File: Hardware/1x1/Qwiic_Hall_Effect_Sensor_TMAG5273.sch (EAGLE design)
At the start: 7 parts, among them J1 QWIIC_RIGHT_ANGLE, J2 QWIIC_RIGHT_ANGLE, U1 TMAG5273

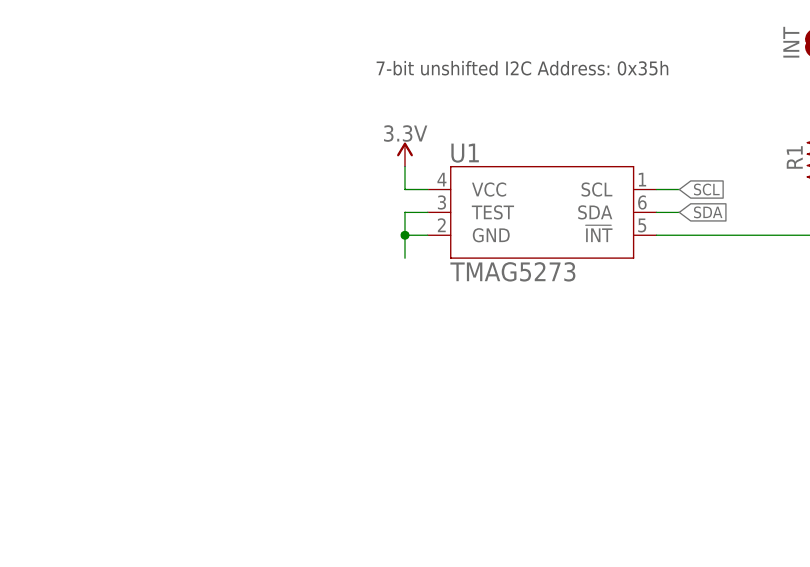
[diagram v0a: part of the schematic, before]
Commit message: Restructured file folders for new board
Added the micro folder and schematic to the project. Moved the 1x1 board into its own file folder.
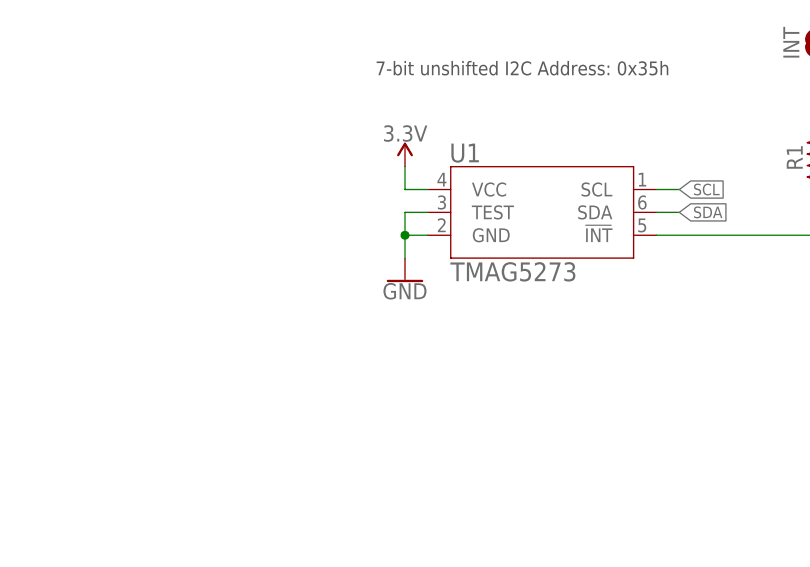
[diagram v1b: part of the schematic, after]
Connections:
- removed net N$1: U1.GND, U1.TEST
- net GND: now also U1.GND, U1.TEST
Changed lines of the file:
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@@
 <part name="SUPPLY5" library="SparkFun-PowerSymbols" deviceset="3.3V" device=""/>
 <part name="GND3" library="SparkFun-PowerSymbols" deviceset="GND" device=""/>
+<part name="GND4" library="SparkFun-PowerSymbols" deviceset="GND" device=""/>
 </parts>
 <sheets>
@@
 <attribute name="VALUE" x="175.26" y="124.206" size="1.778" layer="96" font="vector" align="top-center"/>
 </instance>
+<instance part="GND4" gate="1" x="106.68" y="127" smashed="yes">
+<attribute name="VALUE" x="106.68" y="126.746" size="1.778" layer="96" font="vector" align="top-center"/>
+</instance>
 </instances>
 <busses>
@@
 <wire x1="175.26" y1="127" x2="175.26" y2="128.016" width="0.1524" layer="91"/>
 </segment>
-</net>
-<net name="N$1" class="0">
 <segment>
 <pinref part="U1" gate="A" pin="TEST"/>
@@
 <wire x1="106.68" y1="132.08" x2="106.68" y2="129.54" width="0.1524" layer="91"/>
 <junction x="106.68" y="132.08"/>
+<pinref part="GND4" gate="1" pin="GND"/>
 </segment>
 </net>

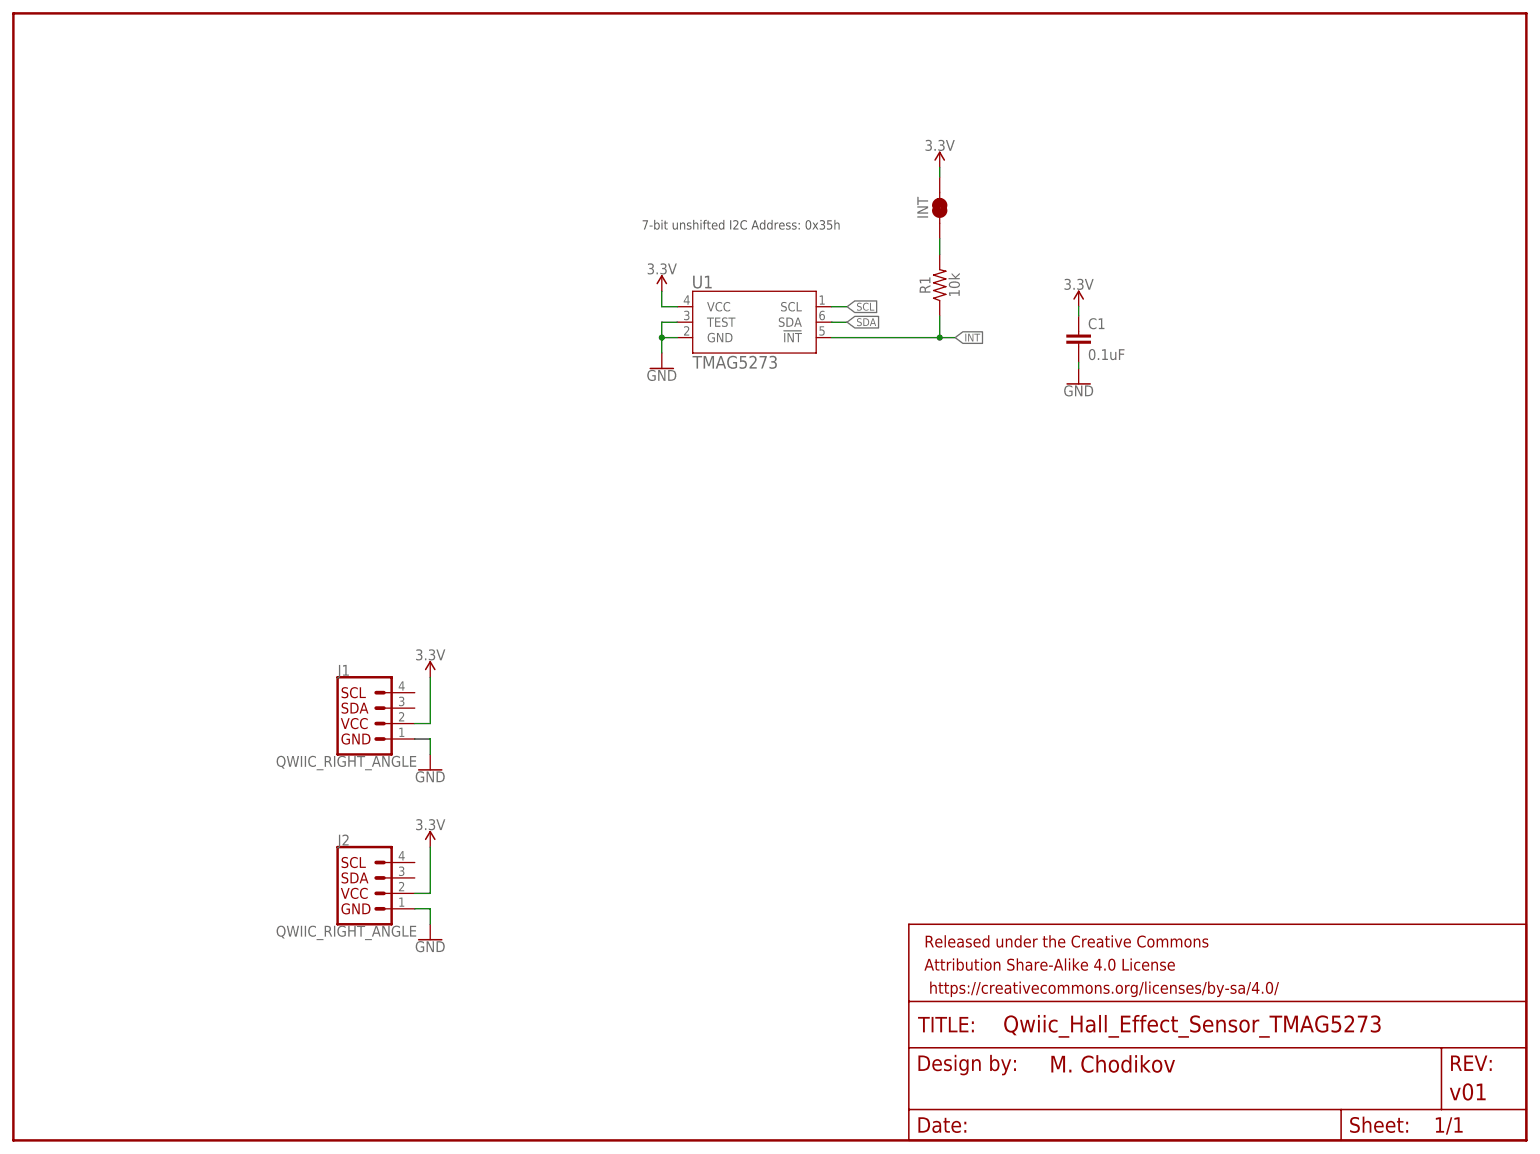
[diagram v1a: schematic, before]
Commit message: Completed schematic and routing
Need to finish aesthetics and dimensions to layout. Almost ready for review.
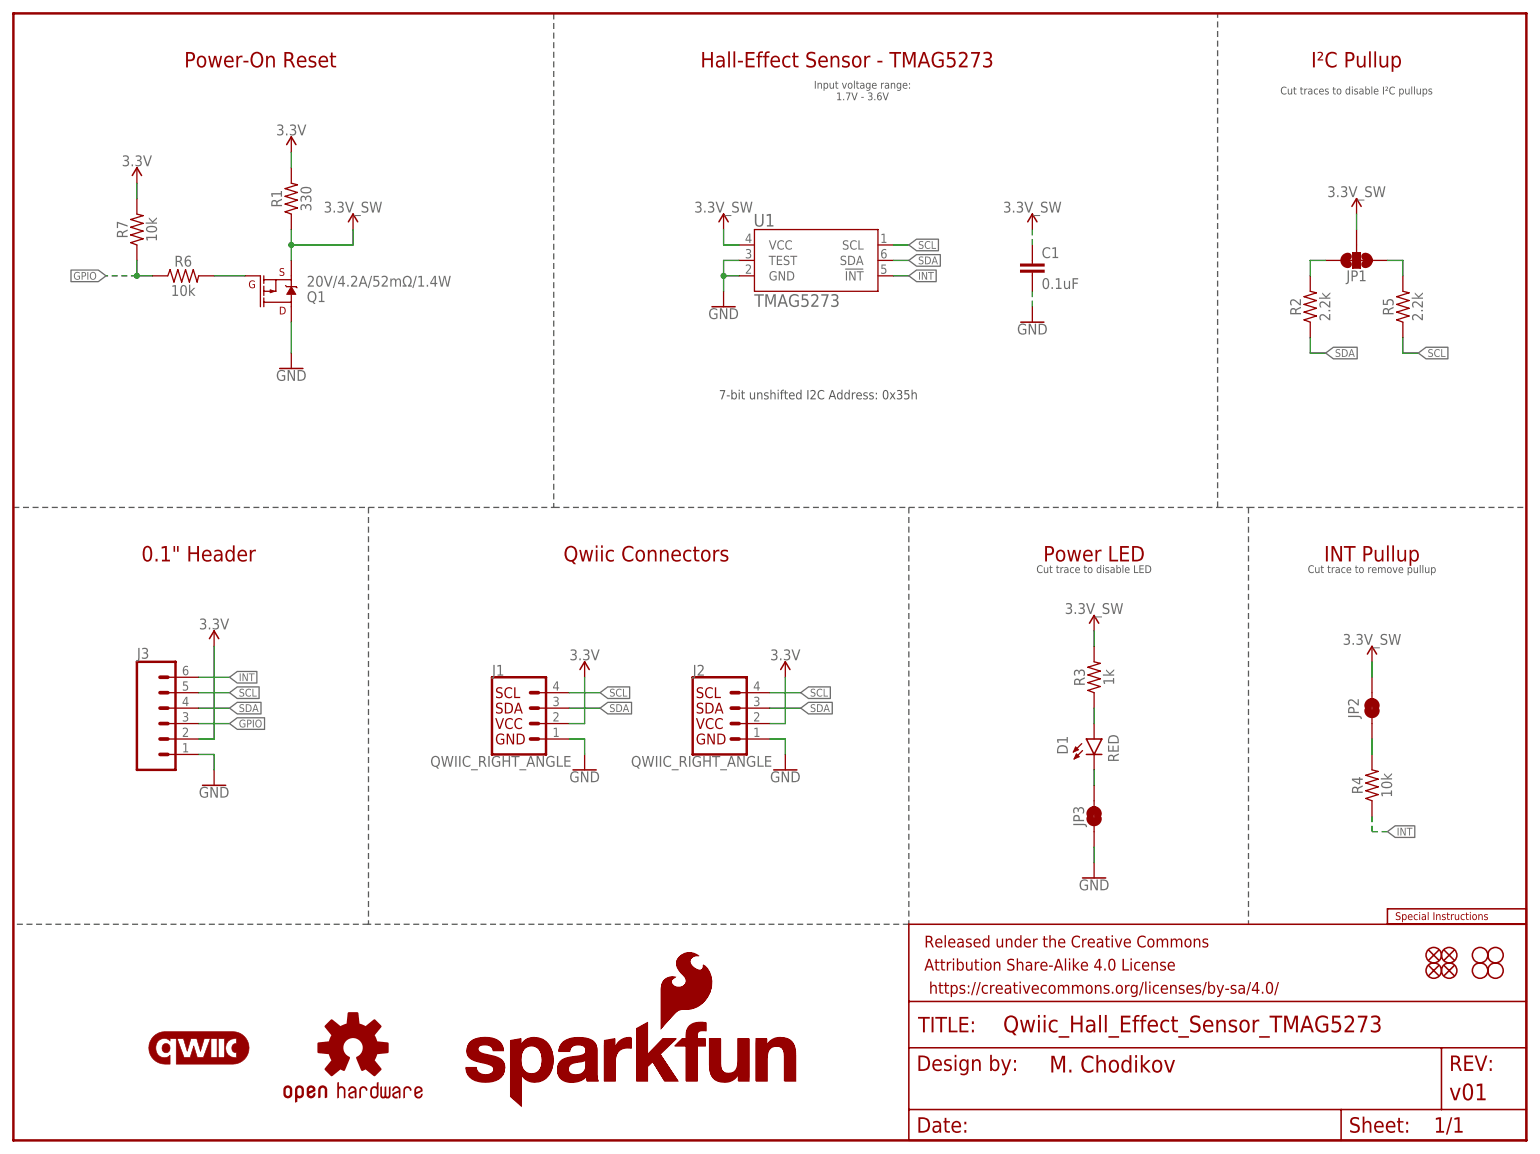
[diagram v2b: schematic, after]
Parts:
- removed INT: JUMPER-SMT_2_NC_TRACE_SILK, SparkFun-Jumpers:JUMPER-SMT_2_NC_TRACE_SILK
- added D1: RED, SparkFun-LED:LED-RED0603
- added FD1, FD2, FD3, FD4: FIDUCIAL1X2, SparkFun-Aesthetics:FIDUCIAL1X2
- added H1, H2, H3, H4: STAND-OFF, SparkFun-Hardware:STAND-OFF
- added J3: (no value), SparkFun-Connectors:CONN_06NO_SILK_FEMALE_PTH
- added JP1: JUMPER-SMT_3_2-NC_TRACE_SILK, SparkFun-Jumpers:JUMPER-SMT_3_2-NC_TRACE_SILK
- added JP2, JP3: JUMPER-SMT_2_NC_TRACE_SILK, SparkFun-Jumpers:JUMPER-SMT_2_NC_TRACE_SILK
- added LOGO1: OSHW-LOGOS, SparkFun-Aesthetics:OSHW-LOGOS
- added LOGO2: SFE_LOGO_NAME_FLAME.1_INCH, SparkFun-Aesthetics:SFE_LOGO_NAME_FLAME.1_INCH
- added LOGO3: QWIIC_LOGO_CONNECTOR, SparkFun-Aesthetics:QWIIC_LOGO_CONNECTOR
- added LOGO4: SFE_LOGO_NAME8_MM, SparkFun-Aesthetics:SFE_LOGO_NAME8_MM
- added LOGO5: SPECIAL_INSTRUCTIONS-ORDERING, SparkFun-Aesthetics:SPECIAL_INSTRUCTIONS-ORDERING
- added LOGO6: SFE_LOGO_FLAME.1_INCH, SparkFun-Aesthetics:SFE_LOGO_FLAME.1_INCH
- added Q1: 20V/4.2A/52mΩ/1.4W, SparkFun-DiscreteSemi:MOSFET_PCH-DMG2305UX-7
- added R2, R5: 2.2k, SparkFun-Resistors:2.2KOHM-0603-1/10W-1%
- added R3: 1k, SparkFun-Resistors:1KOHM-0603-1/10W-1%
- added R4, R6, R7: 10k, SparkFun-Resistors:10KOHM-0603-1/10W-1%
- C1: device SparkFun-Capacitors:0.1UF-0402-10V-10%-X7R -> SparkFun-Capacitors:0.1UF-0603-25V-10%-X7R-WE
- R1: value 10k -> 330; device SparkFun-Resistors:10KOHM-0603-1/10W-1% -> SparkFun-Resistors:330OHM-0603-1/10W-1%
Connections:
- removed net N$3: INT.1, R1.2
- new net 3.3V_SW: C1.1, JP1.2, JP2.2, Q1.S, R1.1, R3.2, U1.VCC
- new net GPIO: J3.3, R6.1, R7.1
- new net N$1: D1.C, JP3.2
- new net N$2: JP1.3, R2.2
- new net N$4: D1.A, R3.1
- new net N$5: JP2.1, R4.2
- new net N$6: JP1.1, R5.2
- new net N$7: Q1.G, R6.2
- net 3.3V: now also J3.2, R1.2, R7.2; no longer C1.1, INT.2, U1.VCC
- net GND: now also J3.1, JP3.1, Q1.D
- net INT: now also J3.6, R4.1; no longer R1.1
- net SCL: now also J1.4, J2.4, J3.5, R5.1
- net SDA: now also J1.3, J2.3, J3.4, R2.1
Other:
- note added: "0.1" Header"
- note added: "Cut trace to disable LED"
- note added: "Cut trace to remove pullup"
- note added: "Cut traces to disable I²C pullups"
- note added: "Hall-Effect Sensor - TMAG5273"
- note added: "INT Pullup"
- note added: "Input voltage range: 1.7V - 3.6V"
- note added: "I²C Pullup"
- note added: "Power LED"
- note added: "Power-On Reset"
- note added: "Qwiic Connectors"
- moved on the sheet: C1, J1, J2, R1, U1

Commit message: Updates for design review
Changed LED and associated resistor to have the correct part and value; added dimension lines and further notes on the layout; adjusted aesthetics in schematic to now be the same as each other (minus the change in Qwiic connectors and number of standoffs)
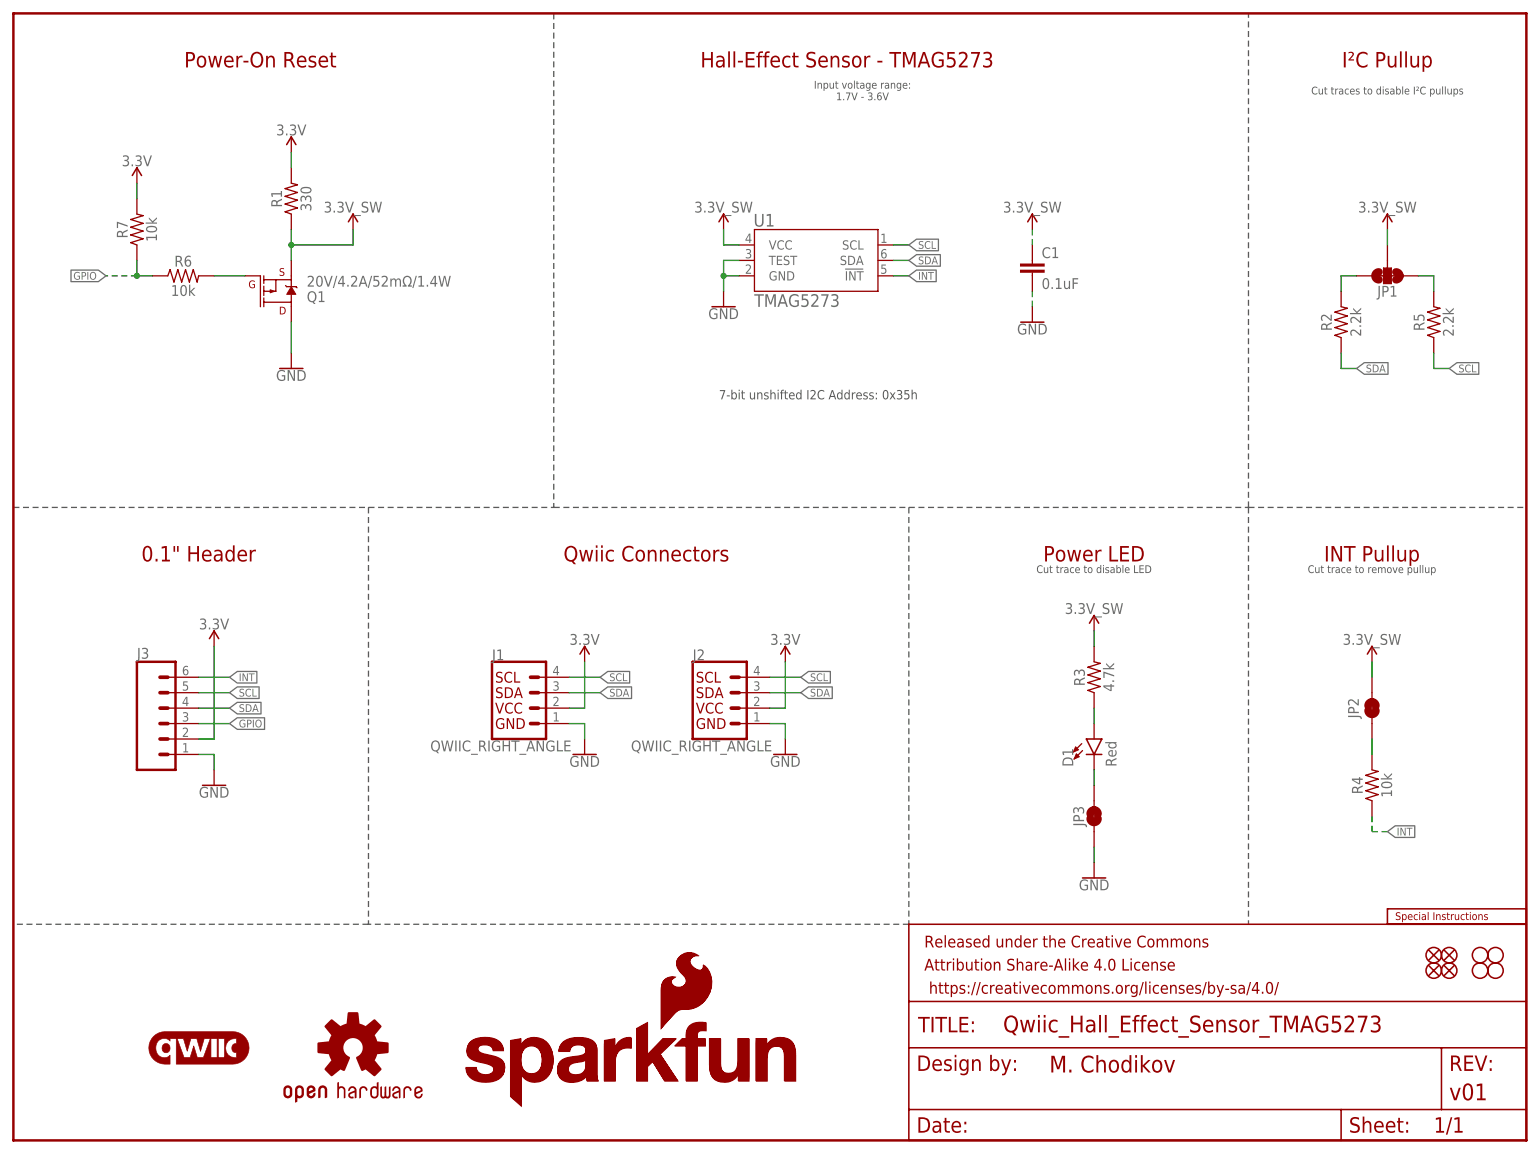
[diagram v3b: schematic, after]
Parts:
- D1: value RED -> Red; device SparkFun-LED:LED-RED0603 -> SparkFun-LED:LED-RED_0603-KB
- R3: value 1k -> 4.7k; device SparkFun-Resistors:1KOHM-0603-1/10W-1% -> SparkFun-Resistors:4.7KOHM-0603-1/10W-1%
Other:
- moved on the sheet: J1, J2, JP1, R2, R5
